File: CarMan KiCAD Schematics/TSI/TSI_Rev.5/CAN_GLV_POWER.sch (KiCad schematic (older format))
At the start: 42 parts, among them K2 G5LE-1-E, K3 SFS2-DC24V, K4 SFS2-DC24V, Q11 TN2130K1-G, U14 Bottom Left, U15 Top Left, U17 Top Right, U2 Bottom Right, U20 511-HCF40106YM013TR, U24 TLP293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

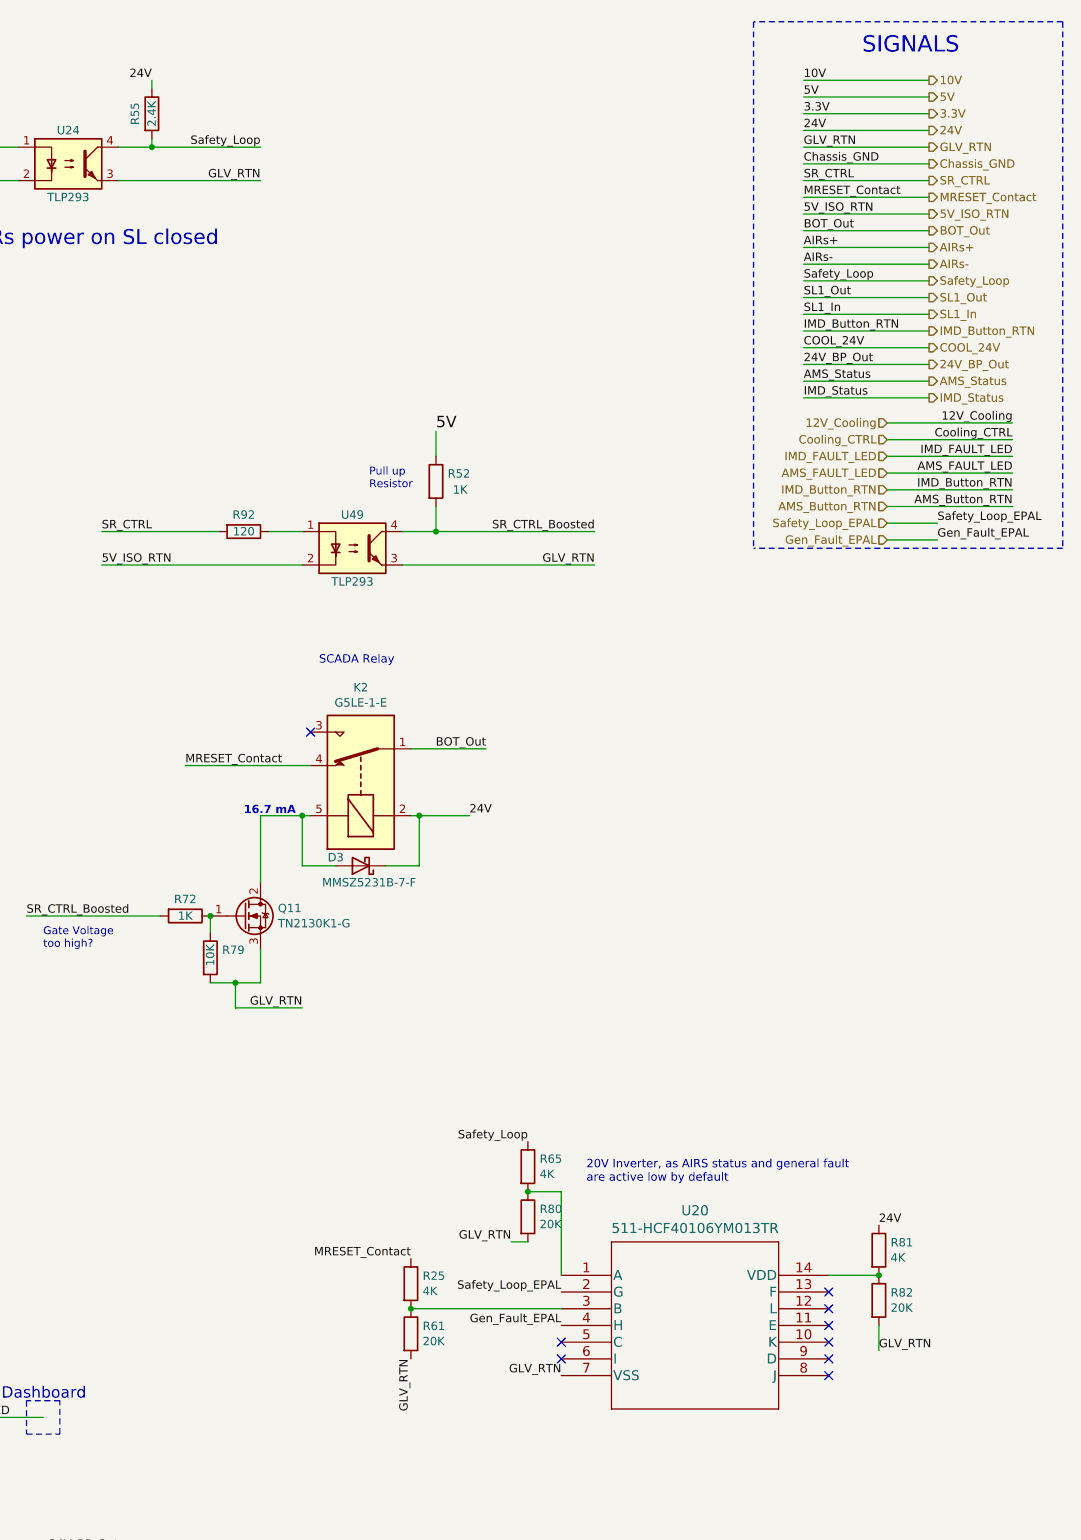
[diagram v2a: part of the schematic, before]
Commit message: TSI removed inverter and made SL and Fault signals Active High using opto isolator for sch and pcb
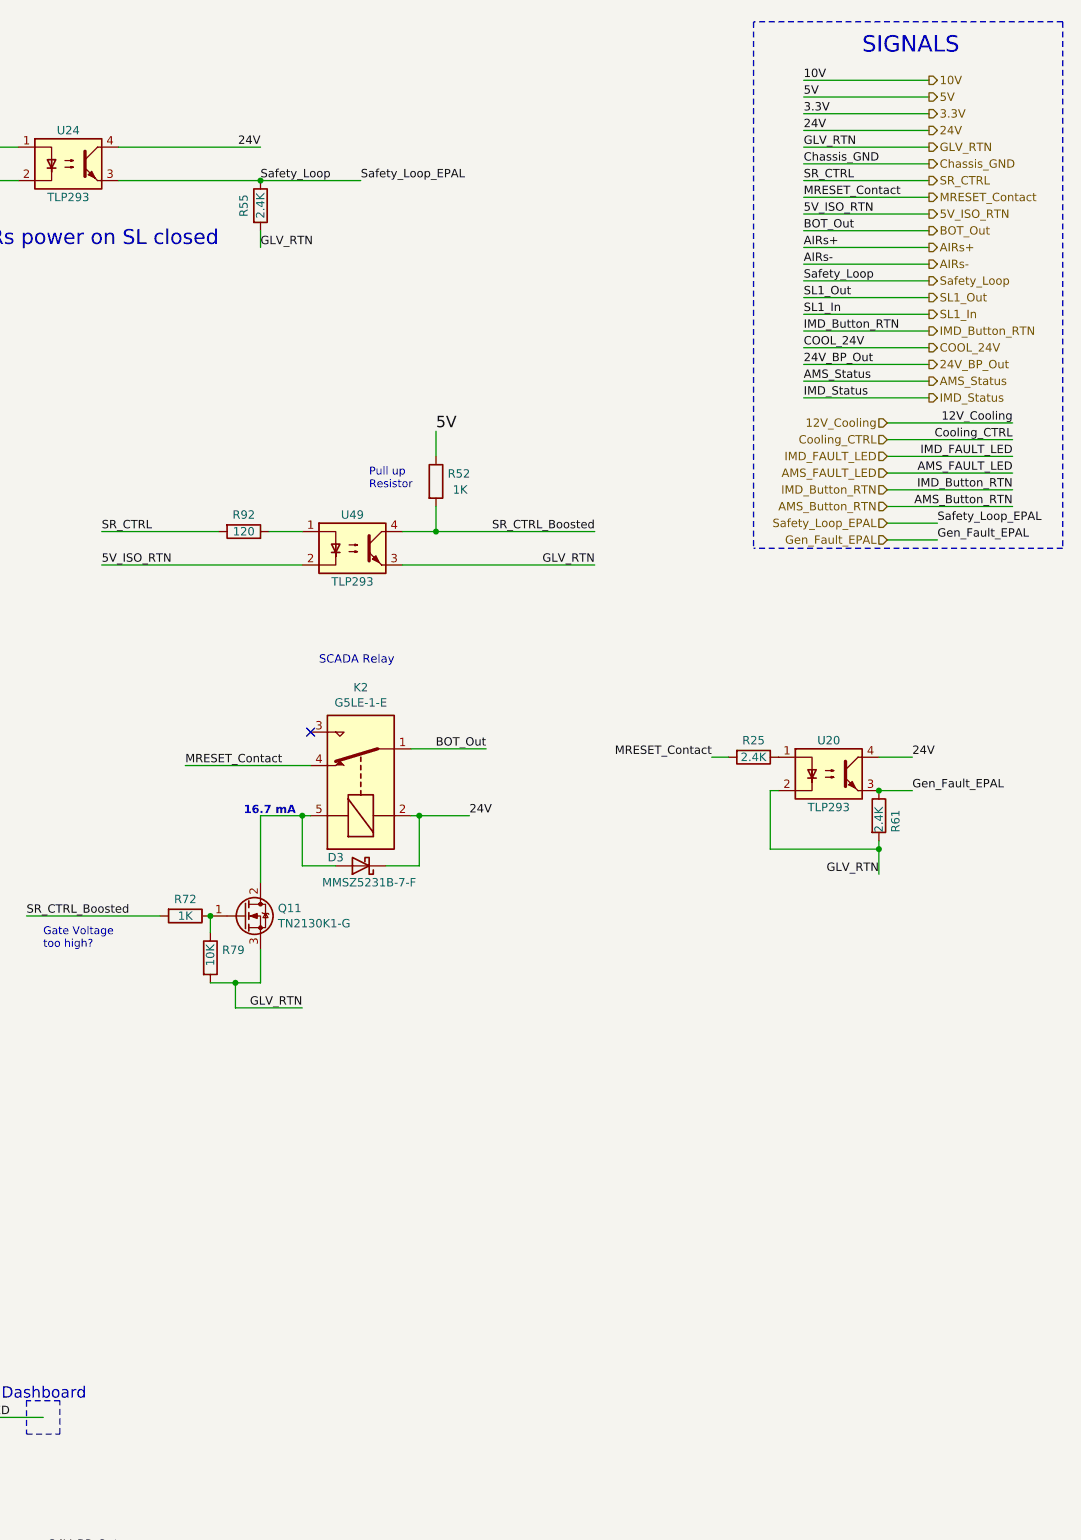
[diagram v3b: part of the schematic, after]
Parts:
- removed R65, R81: 4K, Resistor_SMD:R_0805_2012Metric_Pad1.15x1.40mm_HandSolder, symbol Device:R
- removed R80, R82: 20K, Resistor_SMD:R_0805_2012Metric_Pad1.15x1.40mm_HandSolder, symbol Device:R
- removed U20: 511-HCF40106YM013TR, CarMan General Footprints:511-HCF40106YM013TR, symbol CarMan_KiCAD_Library:511-HCF40106YM013TR
- added U20: TLP293, Package_SO:SOIC-4_4.55x2.6mm_P1.27mm, symbol TSI_Rev.5-rescue:TLP293-CarMan_KiCAD_Library-TSI_Rev.5-rescue
- R25: value 4K -> 2.4K
- R61: value 20K -> 2.4K
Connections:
- wire segments 182 -> 183
- no-connect marks 17 -> 9
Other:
- note removed: "20V Inverter, as AIRS status and general fault\nare active low by default"
- moved on the sheet: R55
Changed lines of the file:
@@
 	0    1    1    0
 $EndComp
-Text Label 11200 1500 2    50   ~ 0
-GLV_RTN
 $Comp
 L Device:R R55
 U 1 1 5FB65AC4
-P 10550 1100
-F 0 "R55" V 10450 1100 50  0000 C CNN
-F 1 "2.4K" V 10550 1100 50  0000 C CNN
-F 2 "Resistor_SMD:R_0805_2012Metric_Pad1.15x1.40mm_HandSolder" V 10480 1100 50  0001 C CNN
-F 3 "~" H 10550 1100 50  0001 C CNN
-	1    10550 1100
+P 11200 1650
+F 0 "R55" V 11100 1650 50  0000 C CNN
+F 1 "2.4K" V 11200 1650 50  0000 C CNN
+F 2 "Resistor_SMD:R_0805_2012Metric_Pad1.15x1.40mm_HandSolder" V 11130 1650 50  0001 C CNN
+F 3 "~" H 11200 1650 50  0001 C CNN
+	1    11200 1650
 	1    0    0    -1
 $EndComp
@@
 Wire Wire Line
 	10350 1500 11200 1500
+Text Label 11200 1500 0    50   ~ 0
+Safety_Loop
 Text Label 11200 1300 2    50   ~ 0
-Safety_Loop
-Text Label 10550 900  2    50   ~ 0
 24V
-Wire Wire Line
-	10350 1300 10550 1300
-Wire Wire Line
-	10550 1300 10550 1250
-Connection ~ 10550 1300
-Wire Wire Line
-	10550 950  10550 900
-Wire Wire Line
-	10550 1300 11200 1300
 Wire Wire Line
 	11050 6300 11050 6450
@@
 Wire Notes Line
 	2950 650  2950 3250
-$Comp
-L CarMan_KiCAD_Library:511-HCF40106YM013TR U20
-U 1 1 60107413
-P 13000 8050
-F 0 "U20" H 13800 8437 60  0000 C CNN
-F 1 "511-HCF40106YM013TR" H 13800 8331 60  0000 C CNN
-F 2 "CarMan General Footprints:511-HCF40106YM013TR" H 13800 8290 60  0001 C CNN
-F 3 "https://www.mouser.com/datasheet/2/389/hcf40106-954733.pdf" H 13800 8331 60  0001 C CNN
-	1    13000 8050
-	1    0    0    -1
-$EndComp
-$Comp
-L Device:R R81
-U 1 1 60112B09
-P 14900 7900
-F 0 "R81" H 14970 7946 50  0000 L CNN
-F 1 "4K" H 14970 7855 50  0000 L CNN
-F 2 "Resistor_SMD:R_0805_2012Metric_Pad1.15x1.40mm_HandSolder" V 14830 7900 50  0001 C CNN
-F 3 "~" H 14900 7900 50  0001 C CNN
-	1    14900 7900
-	1    0    0    -1
-$EndComp
-$Comp
-L Device:R R82
-U 1 1 60113131
-P 14900 8200
-F 0 "R82" H 14970 8246 50  0000 L CNN
-F 1 "20K" H 14970 8155 50  0000 L CNN
-F 2 "Resistor_SMD:R_0805_2012Metric_Pad1.15x1.40mm_HandSolder" V 14830 8200 50  0001 C CNN
-F 3 "~" H 14900 8200 50  0001 C CNN
-	1    14900 8200
-	1    0    0    -1
-$EndComp
-Text Label 14900 7750 0    50   ~ 0
-24V
-Text Label 14900 8500 0    50   ~ 0
-GLV_RTN
-Wire Wire Line
-	14900 8350 14900 8500
-Wire Wire Line
-	14600 8050 14900 8050
-Connection ~ 14900 8050
-Text Label 13000 8650 2    50   ~ 0
-GLV_RTN
-Text Label 12800 7250 2    50   ~ 0
-Safety_Loop
-Text Label 12100 7950 2    50   ~ 0
+Text Label 13900 4950 2    50   ~ 0
 MRESET_Contact
 Text HLabel 14950 3550 0    50   Input ~ 0
@@
 Wire Wire Line
 	14950 3650 15250 3650
-Text Label 13000 8350 2    50   ~ 0
+Text Label 15100 5150 0    50   ~ 0
 Gen_Fault_EPAL
-Text Label 13000 8150 2    50   ~ 0
+Wire Notes Line
+	16000 3700 14150 3700
+Wire Notes Line
+	16000 550  16000 3700
+Wire Notes Line
+	14150 550  14150 3700
+Wire Wire Line
+	10350 1300 11200 1300
+Text Label 11200 1900 0    50   ~ 0
+GLV_RTN
+Wire Wire Line
+	11200 1800 11200 1900
+Text Label 11800 1500 0    50   ~ 0
 Safety_Loop_EPAL
-NoConn ~ 13000 8450
-NoConn ~ 13000 8550
-NoConn ~ 14600 8650
-NoConn ~ 14600 8550
-NoConn ~ 14600 8450
-NoConn ~ 14600 8350
-NoConn ~ 14600 8250
-NoConn ~ 14600 8150
-$Comp
-L Device:R R65
-U 1 1 601AB819
-P 12800 7400
-F 0 "R65" H 12870 7446 50  0000 L CNN
-F 1 "4K" H 12870 7355 50  0000 L CNN
-F 2 "Resistor_SMD:R_0805_2012Metric_Pad1.15x1.40mm_HandSolder" V 12730 7400 50  0001 C CNN
-F 3 "~" H 12800 7400 50  0001 C CNN
-	1    12800 7400
-	1    0    0    -1
-$EndComp
-$Comp
-L Device:R R80
-U 1 1 601AB823
-P 12800 7700
-F 0 "R80" H 12870 7746 50  0000 L CNN
-F 1 "20K" H 12870 7655 50  0000 L CNN
-F 2 "Resistor_SMD:R_0805_2012Metric_Pad1.15x1.40mm_HandSolder" V 12730 7700 50  0001 C CNN
-F 3 "~" H 12800 7700 50  0001 C CNN
-	1    12800 7700
+Wire Wire Line
+	11200 1500 11800 1500
+Connection ~ 11200 1500
+$Comp
+L TSI_Rev.5-rescue:TLP293-CarMan_KiCAD_Library-TSI_Rev.5-rescue U20
+U 1 1 6012F5F3
+P 14600 5050
+F 0 "U20" H 14600 5250 50  0000 C CNN
+F 1 "TLP293" H 14600 4850 50  0000 C CNN
+F 2 "Package_SO:SOIC-4_4.55x2.6mm_P1.27mm" H 14400 4850 50  0001 L CIN
+F 3 "https://www.mouser.com/ProductDetail/Toshiba/TLP293GB-TPLE/?qs=OLJpxlzHOSSc5RAOktTSWw%3D%3D" H 14600 5050 50  0001 L CNN
+	1    14600 5050
 	1    0    0    -1
 $EndComp
 $Comp
 L Device:R R25
-U 1 1 601C082D
-P 12100 8100
-F 0 "R25" H 12170 8146 50  0000 L CNN
-F 1 "4K" H 12170 8055 50  0000 L CNN
-F 2 "Resistor_SMD:R_0805_2012Metric_Pad1.15x1.40mm_HandSolder" V 12030 8100 50  0001 C CNN
-F 3 "~" H 12100 8100 50  0001 C CNN
-	1    12100 8100
-	1    0    0    -1
+U 1 1 60131E61
+P 14150 4950
+F 0 "R25" V 14050 4950 50  0000 C CNN
+F 1 "2.4K" V 14150 4950 50  0000 C CNN
+F 2 "Resistor_SMD:R_0805_2012Metric_Pad1.15x1.40mm_HandSolder" V 14080 4950 50  0001 C CNN
+F 3 "~" H 14150 4950 50  0001 C CNN
+	1    14150 4950
+	0    1    1    0
 $EndComp
 $Comp
 L Device:R R61
-U 1 1 601C0837
-P 12100 8400
-F 0 "R61" H 12170 8446 50  0000 L CNN
-F 1 "20K" H 12170 8355 50  0000 L CNN
-F 2 "Resistor_SMD:R_0805_2012Metric_Pad1.15x1.40mm_HandSolder" V 12030 8400 50  0001 C CNN
-F 3 "~" H 12100 8400 50  0001 C CNN
-	1    12100 8400
-	1    0    0    -1
-$EndComp
-Text Label 12100 8550 3    50   ~ 0
-GLV_RTN
-Text Label 12700 7850 2    50   ~ 0
-GLV_RTN
-Wire Wire Line
-	12800 7850 12700 7850
-Wire Wire Line
-	12800 7550 13000 7550
-Wire Wire Line
-	13000 7550 13000 8050
-Connection ~ 12800 7550
-Wire Wire Line
-	12100 8250 13000 8250
-Connection ~ 12100 8250
-Text Notes 13150 7500 0    50   ~ 0
-20V Inverter, as AIRS status and general fault\nare active low by default
-Wire Notes Line
-	16000 3700 14150 3700
-Wire Notes Line
-	16000 550  16000 3700
-Wire Notes Line
-	14150 550  14150 3700
+U 1 1 601328F4
+P 14900 5300
+F 0 "R61" V 15000 5200 50  0000 L CNN
+F 1 "2.4K" V 14900 5200 50  0000 L CNN
+F 2 "Resistor_SMD:R_0805_2012Metric_Pad1.15x1.40mm_HandSolder" V 14830 5300 50  0001 C CNN
+F 3 "~" H 14900 5300 50  0001 C CNN
+	1    14900 5300
+	1    0    0    -1
+$EndComp
+Wire Wire Line
+	14000 4950 13900 4950
+Wire Wire Line
+	14900 4950 15100 4950
+Wire Wire Line
+	14900 5450 14900 5500
+Wire Wire Line
+	14900 5150 15100 5150
+Connection ~ 14900 5150
+Text Label 15100 4950 0    50   ~ 0
+24V
+Text Label 14900 5650 2    50   ~ 0
+GLV_RTN
+Wire Wire Line
+	14300 5150 14250 5150
+Wire Wire Line
+	14250 5150 14250 5500
+Wire Wire Line
+	14250 5500 14900 5500
+Connection ~ 14900 5500
+Wire Wire Line
+	14900 5500 14900 5650
 $EndSCHEMATC

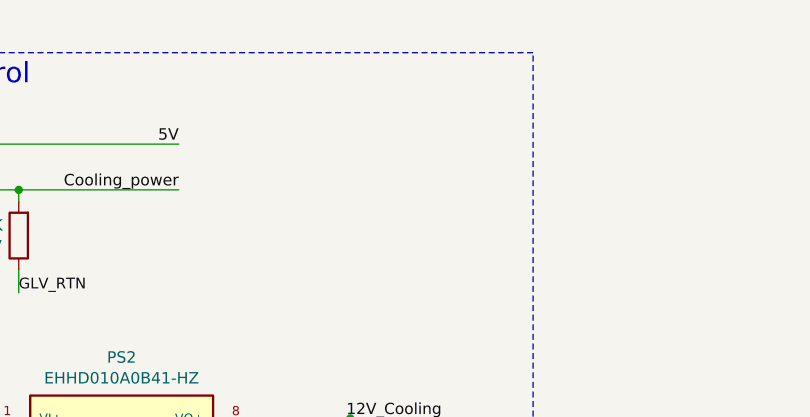
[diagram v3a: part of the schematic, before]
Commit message: Added Cooling Power Jumper to TSI
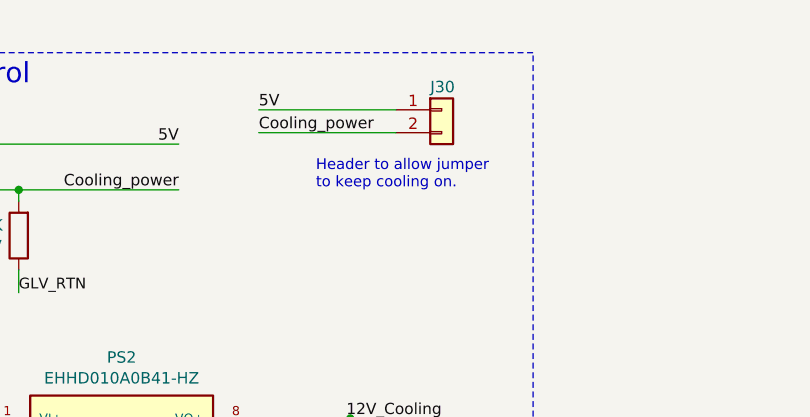
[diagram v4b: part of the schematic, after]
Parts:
- added J30: J23, Connector_PinSocket_2.54mm:PinSocket_1x02_P2.54mm_Vertical, symbol Connector_Generic:Conn_01x02
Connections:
- wire segments 183 -> 185
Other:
- note added: "Header to allow jumper \nto keep cooling on.\n"
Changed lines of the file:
@@
 Wire Wire Line
 	14900 5500 14900 5650
+$Comp
+L Connector_Generic:Conn_01x02 J?
+U 1 1 601DA5ED
+P 7050 900
+AR Path="/601DA5ED" Ref="J?"  Part="1"
+AR Path="/5FE1DE7D/601DA5ED" Ref="J30"  Part="1"
+F 0 "J30" H 7000 1000 50  0000 L CNN
+F 1 "J23" H 7000 1000 50  0001 L CNN
+F 2 "Connector_PinSocket_2.54mm:PinSocket_1x02_P2.54mm_Vertical" H 7050 900 50  0001 C CNN
+F 3 "~" H 7050 900 50  0001 C CNN
+	1    7050 900
+	1    0    0    -1
+$EndComp
+Text Notes 6500 1250 0    47   ~ 0
+Header to allow jumper \nto keep cooling on.\n
+Text Label 6250 1000 0    50   ~ 0
+Cooling_power
+Wire Wire Line
+	6250 1000 6850 1000
+Wire Wire Line
+	6250 900  6850 900
+Text Label 6250 900  0    50   ~ 0
+5V
 $EndSCHEMATC

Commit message: - Updating TSI
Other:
- note added: "Cooling, Relays \nand Voltage Refs\n"
- note removed: "Cooling and Relays\n"
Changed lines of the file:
@@
 Text Notes 7750 4000 2    89   ~ 0
 3.3V REGULATOR
-Text Notes 12450 10350 0    197  ~ 0
-Cooling and Relays\n
+Text Notes 12900 10500 0    177  ~ 0
+Cooling, Relays \nand Voltage Refs\n
 Text Label 10250 3600 0    50   ~ 0
 SR_CTRL

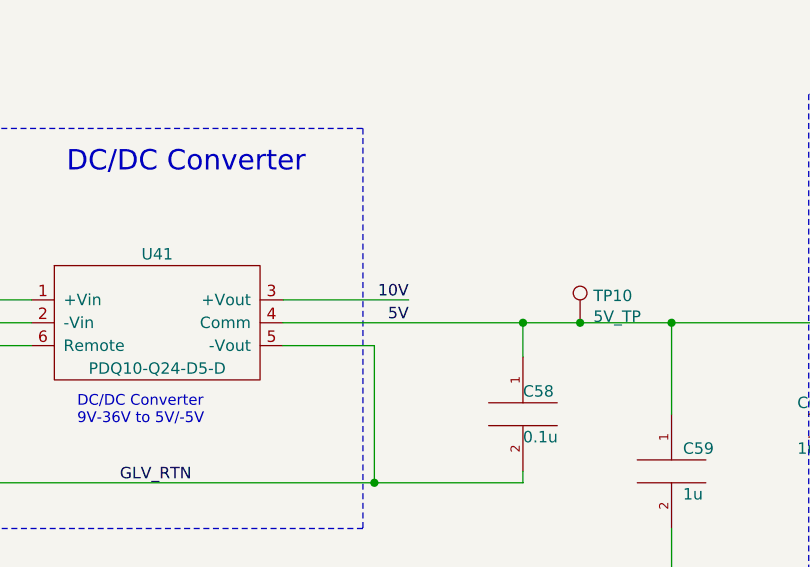
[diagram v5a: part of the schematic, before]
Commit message: Set IGNI_GND to IO_Ground, remove extraneous wire connection, Loaded new netlist
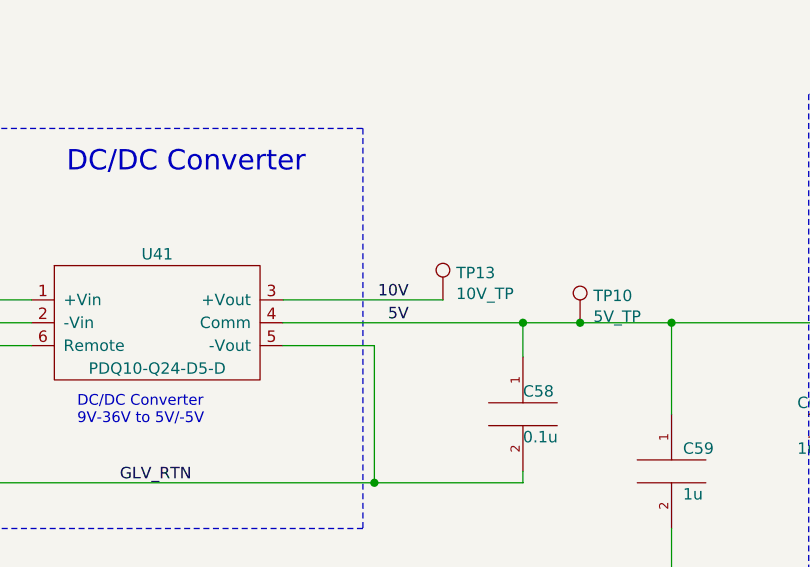
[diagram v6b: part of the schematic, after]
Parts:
- added TP13: 10V_TP, TestPoint:TestPoint_Pad_D3.0mm, symbol Connector:TestPoint
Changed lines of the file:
@@
 $Descr A3 16535 11693
 encoding utf-8
-Sheet 4 6
+Sheet 3 6
 Title ""
 Date ""
@@
 	3650 4800 4700 4800
 Wire Wire Line
-	3650 4700 4200 4700
-Wire Wire Line
 	7900 4800 8100 4800
 Wire Wire Line
@@
 Text Label 6250 900  0    50   ~ 0
 5V
+$Comp
+L Connector:TestPoint TP13
+U 1 1 6094CA9A
+P 4350 4700
+F 0 "TP13" H 4408 4818 50  0000 L CNN
+F 1 "10V_TP" H 4408 4727 50  0000 L CNN
+F 2 "TestPoint:TestPoint_Pad_D3.0mm" H 4550 4700 50  0001 C CNN
+F 3 "~" H 4550 4700 50  0001 C CNN
+	1    4350 4700
+	1    0    0    -1
+$EndComp
+Wire Wire Line
+	3650 4700 4350 4700
 $EndSCHEMATC
